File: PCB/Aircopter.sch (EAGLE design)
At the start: 45 parts, among them J1 FTDI_DEVICE, M1 WIRELESS-NRF24L01, U1 GY-521MPU6050

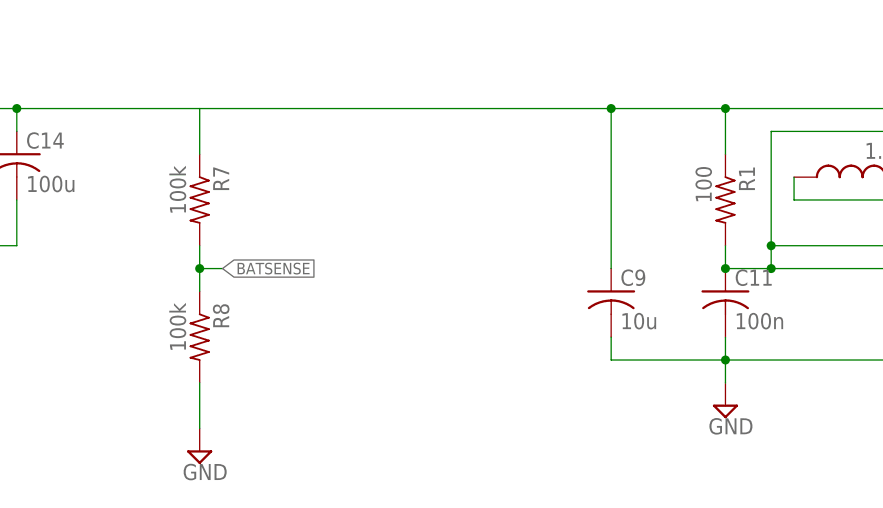
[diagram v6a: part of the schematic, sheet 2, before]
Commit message: Including Jesse's updates to resistor values
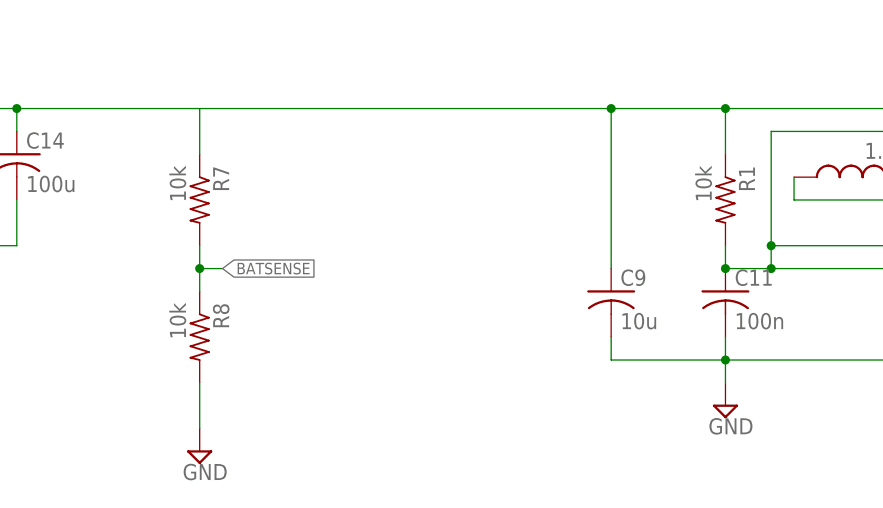
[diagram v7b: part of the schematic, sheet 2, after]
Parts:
- R1: value 100 -> 10k
- R7, R8: value 100k -> 10k
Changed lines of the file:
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@@
 <?xml version="1.0" encoding="utf-8"?>
 <!DOCTYPE eagle SYSTEM "eagle.dtd">
-<eagle version="9.2.1">
+<eagle version="8.4.1">
 <drawing>
 <settings>
@@
 <part name="FRAME2" library="frames" library_urn="urn:adsk.eagle:library:229" deviceset="A3L-LOC" device=""/>
 <part name="L1" library="rcl" library_urn="urn:adsk.eagle:library:334" deviceset="L-US" device="0204/5" package3d_urn="urn:adsk.eagle:package:23488/1" value="1.5u"/>
-<part name="R1" library="rcl" library_urn="urn:adsk.eagle:library:334" deviceset="R-US_" device="R0603" package3d_urn="urn:adsk.eagle:package:23555/2" value="100"/>
+<part name="R1" library="rcl" library_urn="urn:adsk.eagle:library:334" deviceset="R-US_" device="R0603" package3d_urn="urn:adsk.eagle:package:23555/2" value="10k"/>
 <part name="C11" library="rcl" library_urn="urn:adsk.eagle:library:334" deviceset="C-US" device="025-025X050" package3d_urn="urn:adsk.eagle:package:23629/2" value="100n"/>
 <part name="C12" library="rcl" library_urn="urn:adsk.eagle:library:334" deviceset="C-US" device="025-025X050" package3d_urn="urn:adsk.eagle:package:23629/2" value="33u"/>
@@
 <part name="C15" library="rcl" library_urn="urn:adsk.eagle:library:334" deviceset="C-US" device="C0603K" package3d_urn="urn:adsk.eagle:package:23680/2" value="100n"/>
 <part name="SUPPLY15" library="supply2" library_urn="urn:adsk.eagle:library:372" deviceset="GND" device=""/>
-<part name="R7" library="rcl" library_urn="urn:adsk.eagle:library:334" deviceset="R-US_" device="R0603" package3d_urn="urn:adsk.eagle:package:23555/2" value="100k"/>
-<part name="R8" library="rcl" library_urn="urn:adsk.eagle:library:334" deviceset="R-US_" device="R0603" package3d_urn="urn:adsk.eagle:package:23555/2" value="100k"/>
+<part name="R7" library="rcl" library_urn="urn:adsk.eagle:library:334" deviceset="R-US_" device="R0603" package3d_urn="urn:adsk.eagle:package:23555/2" value="10k"/>
+<part name="R8" library="rcl" library_urn="urn:adsk.eagle:library:334" deviceset="R-US_" device="R0603" package3d_urn="urn:adsk.eagle:package:23555/2" value="10k"/>
 <part name="SUPPLY16" library="supply2" library_urn="urn:adsk.eagle:library:372" deviceset="GND" device=""/>
 </parts>
